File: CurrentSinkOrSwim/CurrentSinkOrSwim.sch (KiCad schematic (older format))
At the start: 16 parts

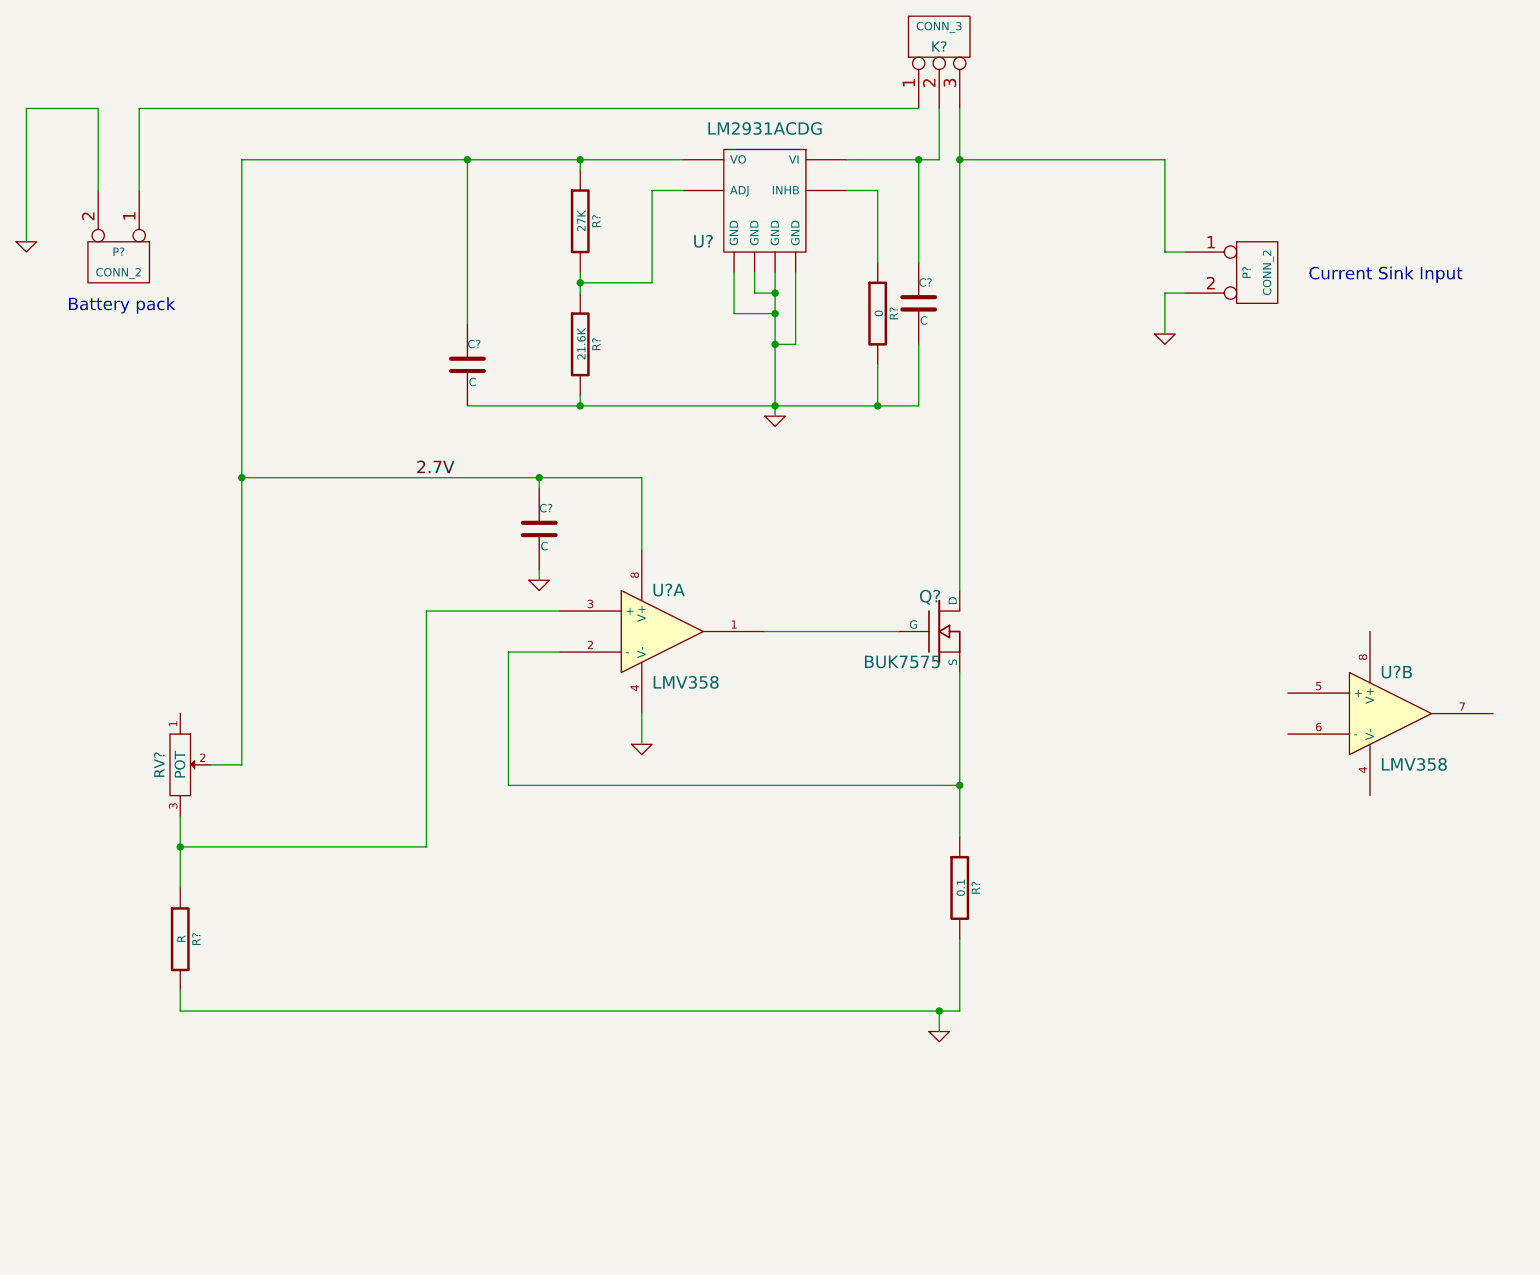
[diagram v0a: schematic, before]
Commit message: adding new sheets
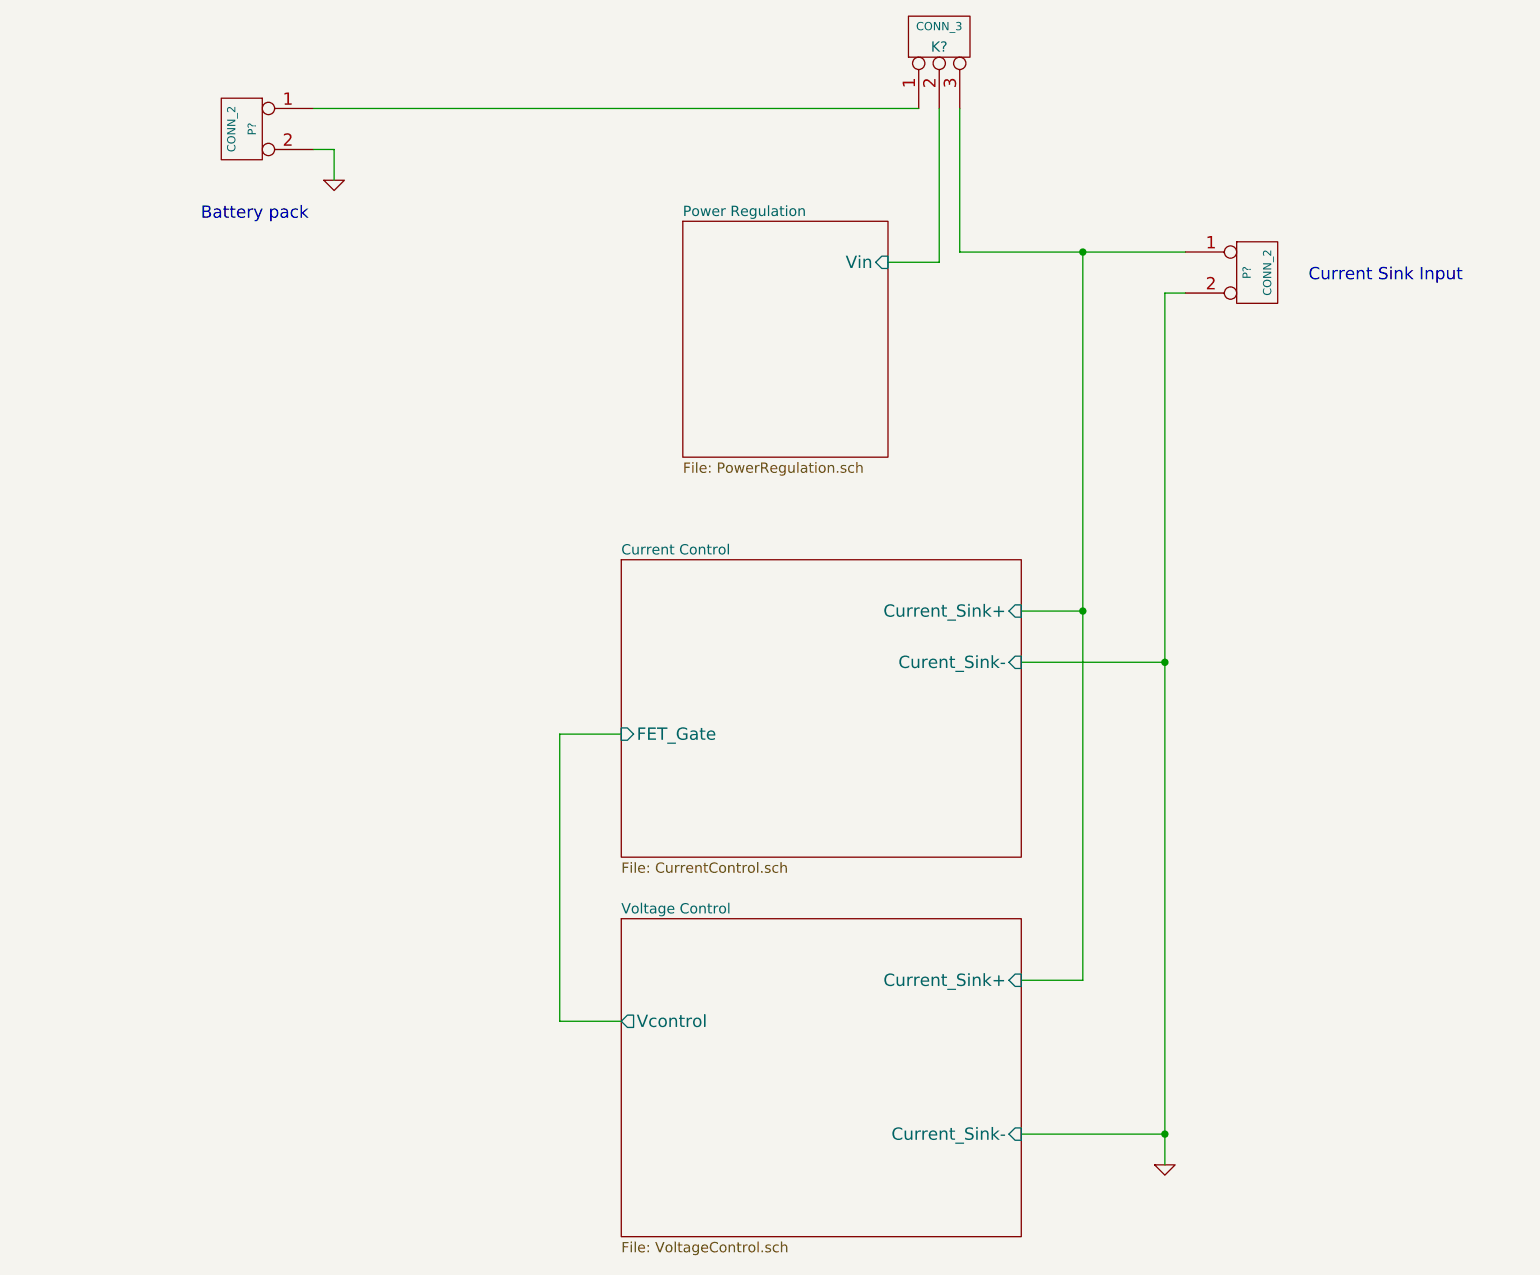
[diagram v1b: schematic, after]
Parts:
- removed C? (x3): C, ~, symbol C
- removed Q?: BUK7575, ~, symbol MOSFET_N
- removed R?: 0.1, ~, symbol R
- removed R?: R, ~, symbol R
- removed R?: 0, ~, symbol R
- removed R?: 27K, ~, symbol R
- removed R?: 21.6K, ~, symbol R
- removed RV?: POT, ~, symbol POT
- removed U? (x2): LMV358, symbol LMV358
- removed U?: LM2931ACDG, ~, symbol LM2931ACDG
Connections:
- net Current Control/Current_Sink+: now reaches K?.3 (P3), P?.1 (P1)
- net Power Regulation/Vin: now reaches K?.2 (PM)
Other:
- moved on the sheet: P?

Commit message: Schematic annotate
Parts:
- gave numbers to parts that had none: 3
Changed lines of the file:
@@
 Sheet 1 4
 Title ""
-Date "1 sep 2015"
+Date "6 sep 2015"
 Rev ""
 Comp ""
@@
 $EndDescr
 $Comp
-L CONN_2 P?
+L CONN_2 P102
 U 1 1 55D77AF4
 P 7600 2150
-F 0 "P?" V 7550 2150 40  0000 C CNN
+F 0 "P102" V 7550 2150 40  0000 C CNN
 F 1 "CONN_2" V 7650 2150 40  0000 C CNN
 F 2 "" H 7600 2150 60  0000 C CNN
@@
 	6150 1350 6150 2050
 $Comp
-L CONN_3 K?
+L CONN_3 K101
 U 1 1 55E488F1
 P 6050 1000
-F 0 "K?" V 6000 1000 50  0000 C CNN
+F 0 "K101" V 6000 1000 50  0000 C CNN
 F 1 "CONN_3" V 6100 1000 40  0000 C CNN
 F 2 "" H 6050 1000 60  0000 C CNN
@@
 $EndComp
 $Comp
-L CONN_2 P?
+L CONN_2 P101
 U 1 1 55E48A06
 P 2650 1450
-F 0 "P?" V 2600 1450 40  0000 C CNN
+F 0 "P101" V 2600 1450 40  0000 C CNN
 F 1 "CONN_2" V 2700 1450 40  0000 C CNN
 F 2 "" H 2650 1450 60  0000 C CNN
@@
 $EndComp
 $Comp
-L GND #PWR?
+L GND #PWR101
 U 1 1 55E48A4E
 P 3100 1700
-F 0 "#PWR?" H 3100 1700 30  0001 C CNN
+F 0 "#PWR101" H 3100 1700 30  0001 C CNN
 F 1 "GND" H 3100 1630 30  0001 C CNN
 F 2 "~" H 3100 1700 60  0000 C CNN
@@
 	4200 4400 4500 4400
 $Comp
-L GND #PWR?
+L GND #PWR102
 U 1 1 55E5F6E4
 P 7150 6500
-F 0 "#PWR?" H 7150 6500 30  0001 C CNN
+F 0 "#PWR102" H 7150 6500 30  0001 C CNN
 F 1 "GND" H 7150 6430 30  0001 C CNN
 F 2 "~" H 7150 6500 60  0000 C CNN

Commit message: Actualizando información de los componentes y creando el BOM
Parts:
- P101, P102: MFG Name (none) -> MA522-500M02
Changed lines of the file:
@@
 Sheet 1 4
 Title ""
-Date "24 sep 2015"
+Date "1 oct 2015"
 Rev ""
 Comp ""
@@
 F 2 "" H 7600 2150 60  0000 C CNN
 F 3 "" H 7600 2150 60  0000 C CNN
+F 4 "MA522-500M02" H 7600 2150 60  0001 C CNN "MFG Name"
 	1    7600 2150
 	1    0    0    -1
@@
 F 2 "" H 2650 1450 60  0000 C CNN
 F 3 "" H 2650 1450 60  0000 C CNN
+F 4 "MA522-500M02" H 2650 1450 60  0001 C CNN "MFG Name"
 	1    2650 1450
 	-1   0    0    -1
